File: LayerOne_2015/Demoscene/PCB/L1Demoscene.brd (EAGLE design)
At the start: 50 x 50 mm, 55 parts, among them IC1 MEGA8-AI, IC2 REG1117, J1 AVR_SPI_PRG_6PTH, J2 CON_HEADER_1X02-PTH

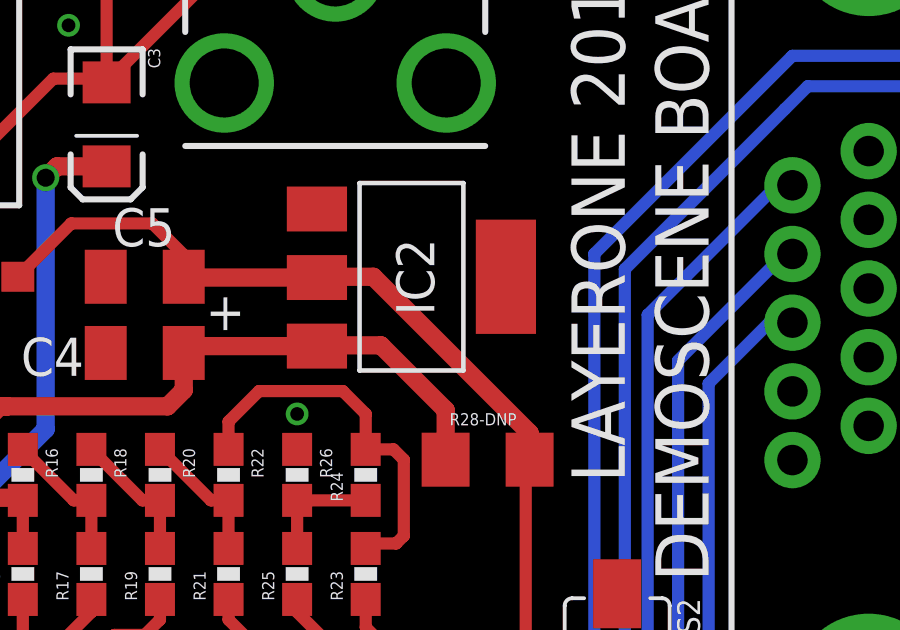
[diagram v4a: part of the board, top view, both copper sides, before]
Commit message: corrected parts #
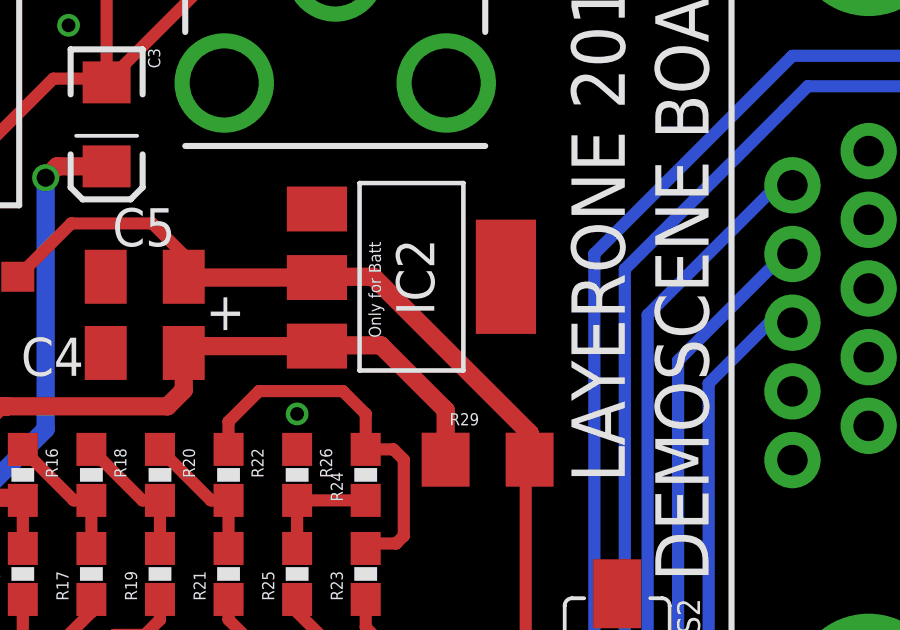
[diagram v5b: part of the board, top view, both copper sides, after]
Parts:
- renumbered R28-DNP to R29
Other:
- board text added: "Only for Batt"
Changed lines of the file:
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@@
 <text x="4.318" y="30.734" size="1.9304" layer="21">+</text>
 <text x="17.272" y="32.512" size="1.27" layer="21">+</text>
+<text x="23.114" y="32.258" size="0.4064" layer="21" rot="R90">Only for Batt</text>
 </plain>
 <attributes>
@@
 <attribute name="NAME" x="23.622" y="35.56" size="1.27" layer="25" ratio="10" rot="R270"/>
 </element>
-<element name="R28-DNP" library="SparkFun-Resistors" package="1206" value="0" x="26.67" y="28.194"/>
+<element name="R29" library="SparkFun-Resistors" package="1206" value="0" x="26.67" y="28.194"/>
 <element name="C4" library="dp_devices" package="SMC_A" value="" x="15.24" y="31.75" smashed="yes" rot="R180">
 <attribute name="NAME" x="13.208" y="32.258" size="1.27" layer="25" font="vector" ratio="10" rot="R180"/>
@@
 <contactref element="R27" pad="2"/>
 <contactref element="IC2" pad="2"/>
-<contactref element="R28-DNP" pad="2"/>
+<contactref element="R29" pad="2"/>
 <contactref element="C5" pad="+"/>
 <contactref element="C6" pad="1"/>
@@
 <contactref element="JP3" pad="VBUS"/>
 <contactref element="IC2" pad="3"/>
-<contactref element="R28-DNP" pad="1"/>
+<contactref element="R29" pad="1"/>
 <contactref element="C4" pad="+"/>
 <wire x1="20.9804" y1="31.9786" x2="21.0058" y2="32.004" width="0.6096" layer="1"/>
